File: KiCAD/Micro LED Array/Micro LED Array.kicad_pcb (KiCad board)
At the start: 2 copper layers, 8.7 x 7.5 mm, 113 parts

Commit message: Working draft
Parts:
- removed D13, D14, D15, D16, D17, D18, D19, D20, D21, D22, D23, D24, D25, D26, D27, D28, D29, D30, D31, D32, D33, D34, D35, D36, D37, D38, D39, D40, D41, D42, D43, D44, D45, D46, D47, D48, D49, D50, D51, D52, D53, D54, D55, D56, D57, D58, D59, D60, D61, D62, D63, D64, D65, D66, D67, D68, D69, D70, D71, D72, D73, D74, D75, D76, D77: LED, Custom footprints:LED_APG0603SEC-E-TT_KNB - with via
- removed H1, H10, H11, H12, H13, H14, H15, H16, H17, H18, H19, H2, H20, H21, H22, H23, H24, H25, H26, H27, H28, H29, H3, H30, H31, H32, H33, H34, H35, H36, H4, H5, H6, H7, H8, H9: Via Pad, Custom footprints:Column Via
- added J1: Conn_02x07_1mm, Custom:2x7 1 mm pitch header, B.Cu at (117.0, 91.5)
- added RN1: 180, Resistor_SMD:R_Array_Convex_8x0602, B.Cu at (117.0, 86.8)
- added RN2: 180, Resistor_SMD:R_Array_Convex_8x0602, B.Cu at (117.0, 96.2)
- D1, D10, D11, D12, D2, D3, D4, D5, D6, D7, D8, D9: footprint Custom footprints:LED_APG0603SEC-E-TT_KNB - with via -> Custom:LED_APG0603SEC-E-TT_KNB
- moved D6 146.6 mm to (118.5, 91.0), turned to 0 degrees
- moved D12 145.9 mm to (117.5, 93.0), turned to 0 degrees
- moved D7 145.4 mm to (115.5, 92.0), turned to 0 degrees
- moved D5 145.3 mm to (117.5, 91.0), turned to 0 degrees
- moved D10 145.0 mm to (118.5, 92.0), turned to 0 degrees
- moved D11 144.6 mm to (116.5, 93.0), turned to 0 degrees
- moved D4 143.9 mm to (116.5, 91.0), turned to 0 degrees
- moved D9 143.7 mm to (117.5, 92.0), turned to 0 degrees
- moved D2 143.0 mm to (117.5, 90.0), turned to 0 degrees
- moved D3 142.6 mm to (115.5, 91.0), turned to 0 degrees
- moved D8 142.4 mm to (116.5, 92.0), turned to 0 degrees
- moved D1 141.7 mm to (116.5, 90.0), turned to 0 degrees
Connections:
- D1 pad 1: /Row1 -> Net-(D1-K)
- D1 pad 2: /Col1 -> /5V
- D10 pad 1: /Row2 -> Net-(D10-K)
- D10 pad 2: /Col3 -> /5V
- D11 pad 1: /Row2 -> Net-(D11-K)
- D11 pad 2: /Col4 -> /5V
- D12 pad 1: /Row2 -> Net-(D12-K)
- D12 pad 2: /Col5 -> /5V
- D2 pad 1: /Row1 -> Net-(D2-K)
- D2 pad 2: /Col2 -> /5V
- D3 pad 1: /Row1 -> Net-(D3-K)
- D3 pad 2: /Col3 -> /5V
- D4 pad 1: /Row1 -> Net-(D4-K)
- D4 pad 2: /Col4 -> /5V
- D5 pad 1: /Row1 -> Net-(D5-K)
- D5 pad 2: /Col5 -> /5V
- D6 pad 1: /Row1 -> Net-(D6-K)
- D6 pad 2: /Col6 -> /5V
- D7 pad 1: /Row1 -> Net-(D7-K)
- D7 pad 2: /Col7 -> /5V
- D8 pad 1: /Row2 -> Net-(D8-K)
- D8 pad 2: /Col1 -> /5V
- D9 pad 1: /Row2 -> Net-(D9-K)
- D9 pad 2: /Col2 -> /5V
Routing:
- net /Row4: track 9.02 -> 0.00 mm, vias 2 -> 0
- net /Row3: track 9.02 -> 0.00 mm, vias 2 -> 0
- net /Row6: track 9.00 -> 0.00 mm, vias 2 -> 0
- net /Row5: track 9.00 -> 0.00 mm, vias 2 -> 0
- net /Row1: track 8.98 -> 0.00 mm, vias 2 -> 0
- net /Row2: track 8.96 -> 0.00 mm, vias 2 -> 0
- net /Row7: track 8.91 -> 0.00 mm, vias 2 -> 0
- net /5V: track 0.00 -> 8.74 mm, vias 0 -> 16
- net /Col8: track 6.65 -> 0.00 mm
- net /Col10: track 6.65 -> 0.00 mm
- net /Col9: track 6.58 -> 0.00 mm
- net /Col11: track 6.41 -> 0.00 mm
- net /Col7: track 6.40 -> 0.00 mm
- net /Col1: track 6.27 -> 0.00 mm
- net /Col2: track 6.27 -> 0.00 mm
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- added copper zone on B.Cu, net /5V
- added copper zone on F.Cu, net /5V
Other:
- board size 8.7 x 7.5 mm -> 8 x 13 mm
- board text added: "+"
- board text added: "-"
- board text added: "."

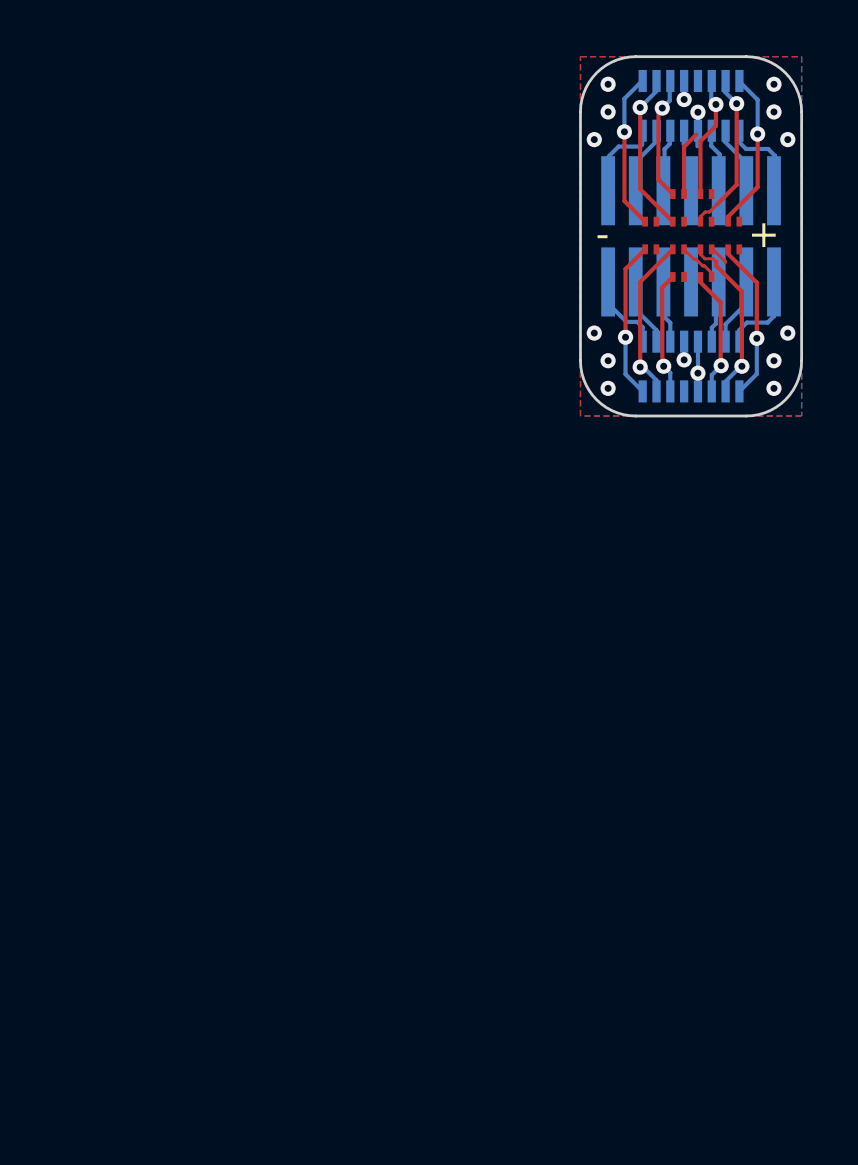
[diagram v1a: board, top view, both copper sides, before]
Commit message: Add holes for electrodes
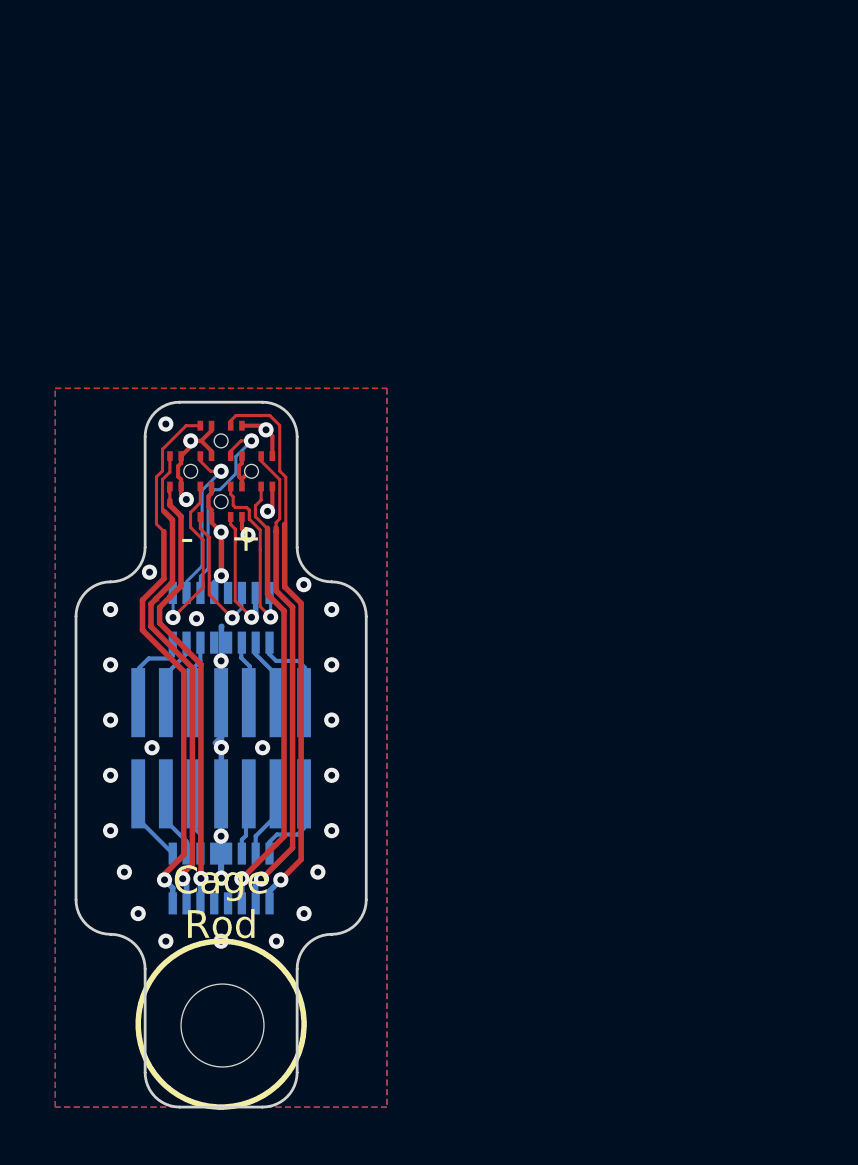
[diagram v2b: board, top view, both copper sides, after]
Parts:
- added REF**: 0.5 mm NPTH, Custom:0.5 mm NPTH, F.Cu at (98.9, 100.0)
- added REF**: 3 mm NPTH, Custom:3 mm NPTH, F.Cu at (100.0, 120.0)
- added REF**: 0.5 mm NPTH, Custom:0.5 mm NPTH, F.Cu at (100.0, 101.1)
- added REF**: 0.5 mm NPTH, Custom:0.5 mm NPTH, F.Cu at (101.1, 100.0)
- added REF**: 0.5 mm NPTH, Custom:0.5 mm NPTH, F.Cu at (100.0, 98.9)
- moved RN2 25.1 mm to (100.0, 114.7)
- moved J1 25.1 mm to (100.0, 110.0)
- moved RN1 25.1 mm to (100.0, 105.3)
- moved D7 19.2 mm to (98.3, 100.5)
- moved D11 19.2 mm to (99.5, 101.7)
- moved D3 19.2 mm to (98.3, 99.5)
- moved D8 19.1 mm to (99.5, 100.5)
- moved D12 19.1 mm to (100.5, 101.7)
- moved D4 19.1 mm to (99.5, 99.5)
- moved D1 19.0 mm to (99.5, 98.3)
- moved D9 19.0 mm to (100.5, 100.5)
- moved D5 19.0 mm to (100.5, 99.5)
- moved D10 18.9 mm to (101.7, 100.5)
- moved D2 18.9 mm to (100.5, 98.3)
- moved D6 18.9 mm to (101.7, 99.5)
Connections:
- RN1 pad 1: Net-(D3-K) -> Net-(D8-K)
- RN1 pad 3: Net-(D1-K) -> Net-(D5-K)
- RN1 pad 6: Net-(D2-K) -> Net-(D11-K)
- RN1 pad 7: Net-(D5-K) -> Net-(D12-K)
- RN1 pad 8: Net-(D6-K) -> Net-(D9-K)
- RN2 pad 1: Net-(D10-K) -> Net-(D2-K)
- RN2 pad 2: Net-(D9-K) -> Net-(D6-K)
- RN2 pad 3: Net-(D12-K) -> Net-(D10-K)
- RN2 pad 6: Net-(D11-K) -> Net-(D7-K)
- RN2 pad 7: Net-(D8-K) -> Net-(D3-K)
- RN2 pad 8: Net-(D7-K) -> Net-(D1-K)
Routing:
- net /5V: track 8.74 -> 30.9 mm, vias 16 -> 34
- net Net-(D2-K): track 4.39 -> 20.3 mm
- net Net-(D1-K): track 4.50 -> 19.7 mm
- net Net-(D3-K): track 5.67 -> 17.4 mm
- net Net-(D6-K): track 5.81 -> 17.3 mm
- net Net-(D7-K): track 5.69 -> 16.4 mm
- net Net-(D10-K): track 5.83 -> 16.2 mm
- net Net-(D5-K): track 5.90 -> 7.47 mm
- net Net-(J1-Pin_7): track 3.17 -> 1.92 mm
- net Net-(D11-K): track 4.42 -> 5.17 mm
- net Net-(J1-Pin_14): track 2.91 -> 3.47 mm
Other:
- board size 8 x 13 mm -> 10.5 x 25.5 mm
- board text added: "- +"
- board text added: "Cage Rod"
- board text removed: "+"
- board text removed: "-"
- board text removed: "."
